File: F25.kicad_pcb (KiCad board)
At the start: 2 copper layers, 45 x 30 mm, 37 parts, among them J3 B2B-PH-K-S, J4 USB_C_Receptacle_USB2.0_16P, Q1 IRLML6244, SW1 RESET, SW2 BOOT, U2 MPU-6050, U3 MS5611-01BA, U4 ESP32-S3-WROOM-1-N8, U5 AP2112K-3.3

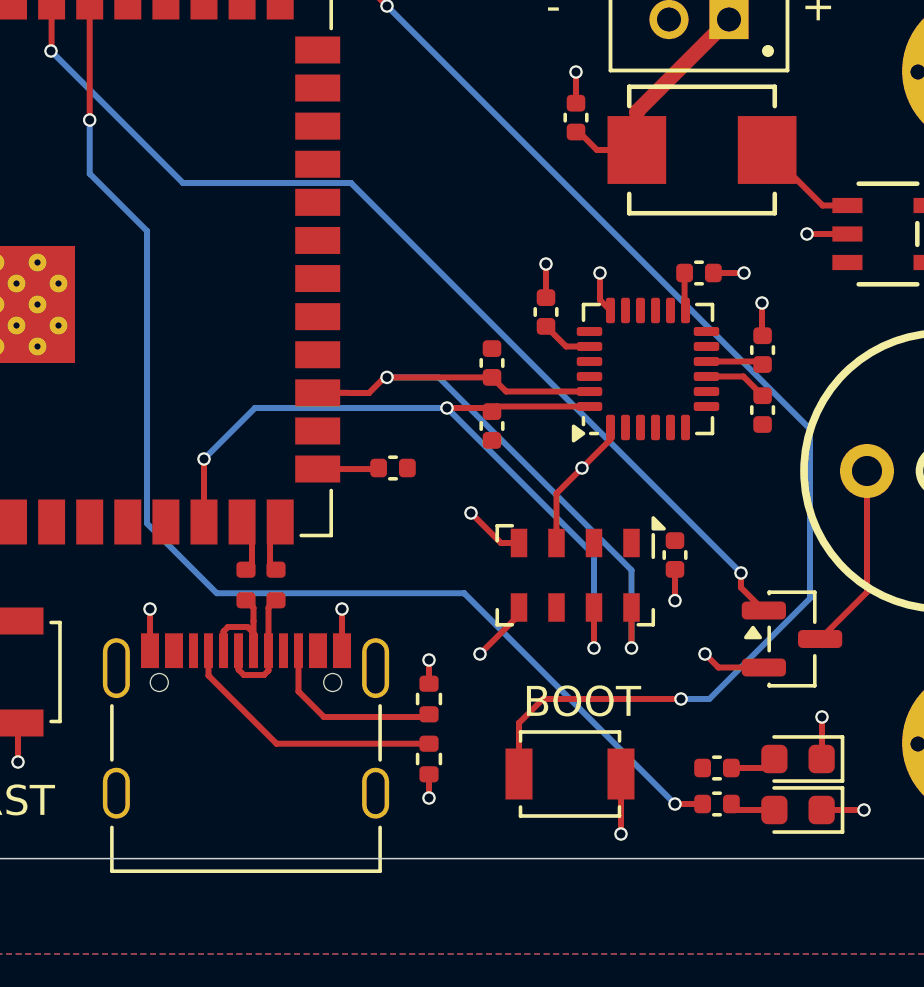
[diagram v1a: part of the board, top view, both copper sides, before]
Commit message: Finish SPI MS6511
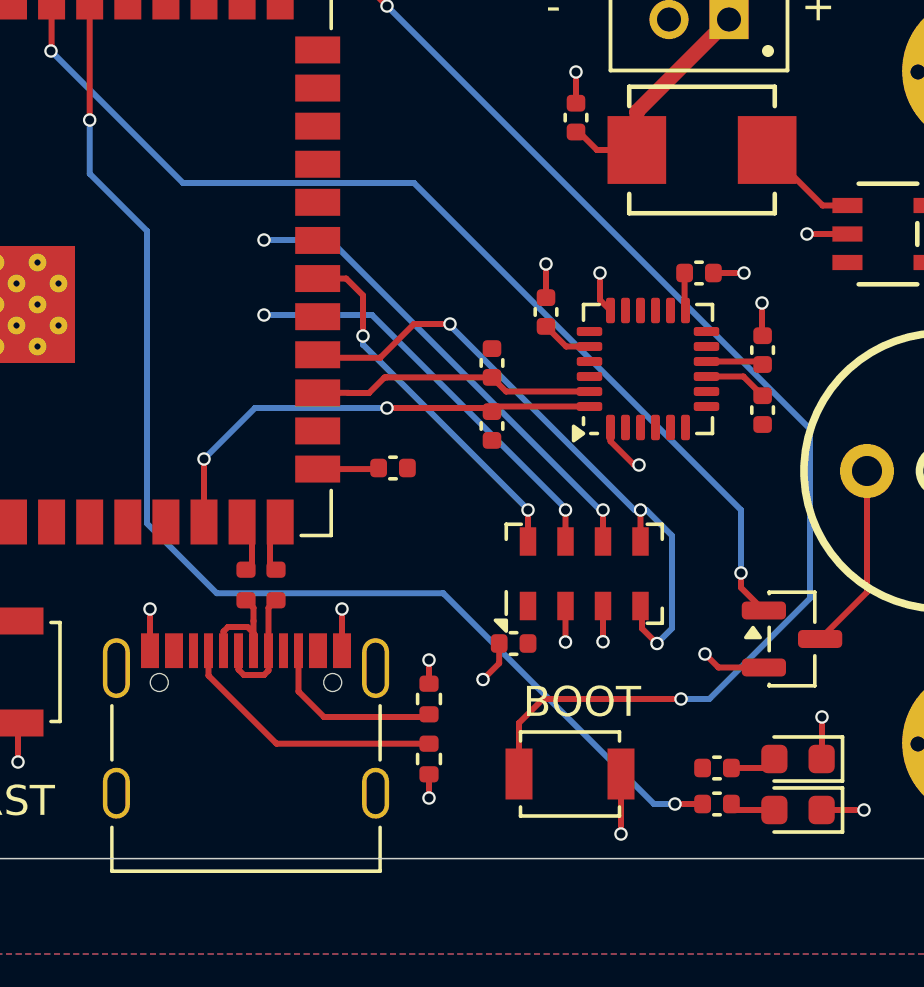
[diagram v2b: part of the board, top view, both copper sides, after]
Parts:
- removed C8: 0.1uF, Capacitor_SMD:C_0402_1005Metric
- removed U3: MS5611-01BA, Package_LGA:LGA-8_3x5mm_P1.25mm
- added C9: 0.1uF, Capacitor_SMD:C_0402_1005Metric, F.Cu at (161.4, 108.2)
- added U1: MS5611-01BA, Package_LGA:LGA-8_3x5mm_P1.25mm, F.Cu at (163.8, 105.8)
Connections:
- U4 pad 18: unconnected-(U4-GPIO10-Pad18) -> /CS
- U4 pad 19: unconnected-(U4-GPIO11-Pad19) -> /MOSI
- U4 pad 20: unconnected-(U4-GPIO12-Pad20) -> /SCK
- U4 pad 21: unconnected-(U4-GPIO13-Pad21) -> /MISO
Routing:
- net /CS: track 0.00 -> 21.5 mm, vias 0 -> 3
- net /MISO: track 0.00 -> 16.1 mm, vias 0 -> 2
- net /SCL: track 24.2 -> 9.47 mm, vias 2 -> 0
- net /MOSI: track 0.00 -> 13.9 mm, vias 0 -> 2
- net /SCK: track 0.00 -> 12.3 mm, vias 0 -> 2
- net /SDA: track 27.4 -> 16.0 mm, vias 3 -> 2
- net BAT-: track 38.3 -> 34.1 mm
- net /BUZZER: track 33.6 -> 34.8 mm

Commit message: Add sponsors
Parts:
- added G***: LOGO, LOGO, B.Cu at (161.7, 91.6)
- added G***: LOGO, LOGO, B.Cu at (156.4, 91.6)
- added G***: LOGO, LOGO, B.Cu at (161.6, 102.6)
- added G***: LOGO, LOGO, B.Cu at (175.2, 100.0)
- added G***: LOGO, LOGO, B.Cu at (143.6, 92.0)
- added G***: LOGO, LOGO, B.Cu at (156.3, 102.1)
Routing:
- net /MOSI: track 13.9 -> 15.8 mm
- net /MISO: track 16.1 -> 17.9 mm

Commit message: Updates
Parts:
- removed the G*** at (175.2, 100.0)
- added G***: LOGO, LOGO, B.Cu at (142.5, 94.6)
- added G***: LOGO, LOGO, B.Cu at (143.1, 89.1)
- added G***: LOGO, LOGO, B.Cu at (147.1, 100.8)
- moved G*** 20.1 mm to (123.8, 95.4), turned to 0 degrees
- moved G*** 13.1 mm to (153.4, 89.3), turned to 0 degrees
- moved G*** 12.8 mm to (151.7, 79.7), turned to 0 degrees
- moved G*** 9.40 mm to (155.0, 95.9), turned to 0 degrees
- moved G*** 7.03 mm to (154.8, 93.1), turned to 0 degrees
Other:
- board text added: "Anthony D."
- board text added: "Fawaaz K.S."
- board text added: "Noah P."

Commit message: Font stuff
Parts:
- removed the G*** at (151.7, 79.7)
- removed the G*** at (123.8, 95.4)
- added ?: , clipboard:8a0a766a-bff8-4b8c-9015-f6a2d7131c27, F.Cu at (172.5, 92.8)
- moved R6 5.92 mm to (158.9, 106.1), turned to -90 degrees
- moved R12 3.96 mm to (157.9, 106.1)
- moved SW1 1.30 mm to (144.8, 107.8), turned to 180 degrees
- moved G*** 0.32 mm to (153.1, 89.3)
- moved G*** 0.20 mm to (143.3, 89.1)
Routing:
- net Net-(J4-CC1): track 9.12 -> 13.3 mm
- net Net-(J4-CC2): track 6.10 -> 8.94 mm
- net /ESP_EN: track 7.53 -> 5.87 mm
- net BAT-: track 34.1 -> 33.1 mm
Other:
- board text added: "MAV"
- board text removed: "Fawaaz K.S."
- board text removed: "Noah P."
